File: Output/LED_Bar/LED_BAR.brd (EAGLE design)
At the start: 20 x 13 mm, 19 parts

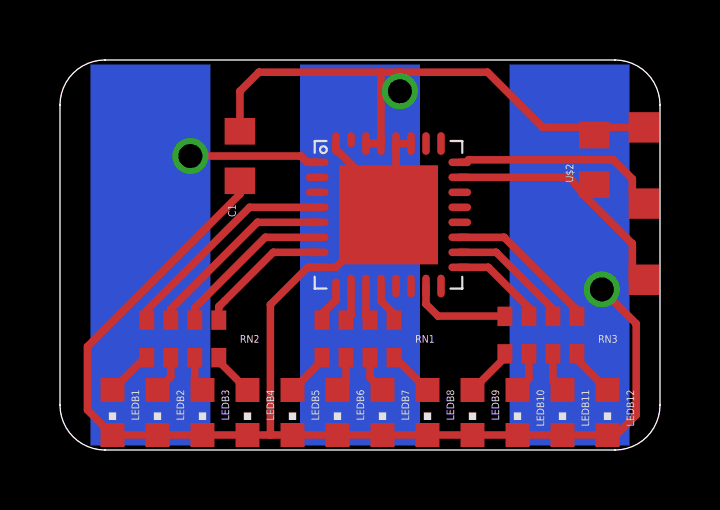
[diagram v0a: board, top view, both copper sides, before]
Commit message: Update Pinheader
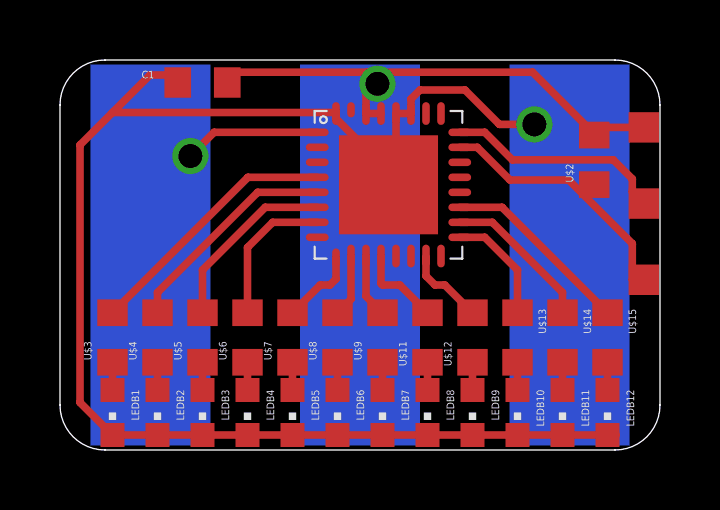
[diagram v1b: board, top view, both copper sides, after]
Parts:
- removed RN1, RN2, RN3: 68, resistor-dil:0603-ARC
- added U$11, U$12, U$13, U$14, U$15, U$3, U$4, U$5, U$6, U$7, U$8, U$9: 68, thar:603
- moved C1 2.75 mm to (6.50, 13.5), turned to 180 degrees
- moved U$10 1.00 mm to (12.7, 10.1)
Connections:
- net GND: no longer U$10.8
- net N$11: now also U$3.2; no longer RN2.8
- net N$13: now also U$6.1; no longer RN2.4
- net N$14: now also U$7.1; no longer RN1.1
- net N$16: now also U$8.1; no longer RN1.2
- net N$17: now also U$4.2; no longer RN2.7
- net N$18: now also U$9.1; no longer RN1.3
- net N$19: now also U$11.1; no longer RN1.4
- net N$20: now also U$12.1; no longer RN3.1
- net N$21: now also U$5.2; no longer RN2.6
- net N$22: now also U$6.2; no longer RN2.5
- net N$23: now also U$7.2; no longer RN1.8
- net N$24: now also U$15.1; no longer RN3.5
- net N$25: now also U$14.1; no longer RN3.6
- net N$26: now also U$8.2; no longer RN1.7
- net N$27: now also U$9.2; no longer RN1.6
- net N$28: now also U$10.15, U$12.2; no longer RN1.5, U$10.12
- net N$29: now also U$10.17, U$13.1; no longer RN3.8, U$10.15
- net N$32: now also LEDB10.A, U$13.2; no longer RN3.7, U$10.17
- net N$34: now also LEDB11.A, U$14.2; no longer LEDB10.A, RN3.2
- net N$35: now also LEDB12.A, U$15.2; no longer LEDB11.A, RN3.3
- net N$36: now also U$10.12, U$11.2; no longer LEDB12.A, RN3.4
- net N$5: now also U$3.1; no longer RN2.1
- net N$6: now also U$4.1; no longer RN2.2
- net N$7: now also U$5.1; no longer RN2.3
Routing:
- net GND: track 52.4 -> 62.7 mm
- net VCC: track 26.1 -> 23.2 mm
- net N$32: track 3.16 -> 0.92 mm
- net N$28: track 1.32 -> 2.72 mm
- net N$23: track 1.27 -> 2.62 mm
- net N$24: track 5.11 -> 6.38 mm
- net N$11: track 7.44 -> 8.69 mm
- net N$36: track 1.63 -> 2.87 mm
- net N$25: track 4.13 -> 5.31 mm
- net N$17: track 6.45 -> 7.38 mm
- net N$27: track 1.19 -> 2.12 mm
- net N$26: track 1.21 -> 2.08 mm
- net N$20: track 1.65 -> 0.92 mm
- net N$5: track 1.59 -> 0.92 mm
- net N$21: track 5.47 -> 6.12 mm
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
